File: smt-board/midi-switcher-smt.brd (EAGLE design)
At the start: 68.6 x 67.3 mm, 70 parts, among them IC1 PIC16F1825DIL14, IC2 6N138, Q1 MJD122GDPAK, Q2 MJD122GDPAK, Q3 MJD122GDPAK, Q4 MJD122GDPAK, Q5 MJD122GDPAK, Q6 MJD122GDPAK, Q7 MJD122GDPAK, Q8 MJD122GDPAK

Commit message: version 7
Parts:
- D1: device adafruit:SOD-123FL -> adafruit:SMADIODE
- moved C4 1.80 mm to (80.0, 57.1)
- moved R1 1.27 mm to (49.5, 41.9)
- moved R5 1.27 mm to (41.9, 41.9)
- moved D2 1.27 mm to (49.5, 44.5)
- moved R4 1.27 mm to (41.9, 44.5)
- moved D1 0.46 mm to (71.5, 54.9)
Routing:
- net N$3: track 13.8 -> 15.0 mm
- net N$2: track 27.0 -> 28.2 mm
- net N$5: track 14.5 -> 15.8 mm
- net N$39: track 21.8 -> 22.9 mm
- net N$1: track 12.1 -> 13.0 mm
- net N$28: track 9.43 -> 10.3 mm
- net N$17: track 29.5 -> 29.0 mm
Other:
- board text added: "rev 7"
- board text removed: "rev 6"

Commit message: new layout
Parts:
- removed JP18, JP19: (no value), adafruit:1X01
- added D3: 1N4004, jasons_stuff:DO-VERT
- added JP1, JP2, POWER+1, POWER+2, POWER-1, POWER-2: (no value), adafruit:1X01
- added JP3: (no value), pinhead:1X03
- added R22: (no value), rcl:R0805
- added T1: (no value), transistor:SOT23-BEC
- added U$1: 2.1MMJACKTHM, adafruit:PJ-102A
- C4: device rcl:PANASONIC_F -> rcl:E2,5-7
- C5: device rcl:PANASONIC_D -> rcl:E2,5-6
- D1: value (none) -> 1N4004; device adafruit:SMADIODE -> jasons_stuff:DO-VERT
- IC1: value PIC16F1825DIL14 -> PIC16F1825SO14; device jasons_stuff:DIL14 -> jasons_stuff:SO14
- moved OP1+ 69.2 mm to (31.8, 7.62)
- moved PWR 56.6 mm to (88.9, 36.8)
- moved ACT 54.6 mm to (85.1, 36.8)
- moved C2 39.9 mm to (100.3, 15.2), turned to 270 degrees
- moved OP5+ 39.4 mm to (72.4, 7.62)
- moved R4 37.9 mm to (78.7, 35.6), turned to 0 degrees
- moved R1 37.7 mm to (17.8, 21.6)
- moved R5 37.0 mm to (78.7, 38.1), turned to 180 degrees
- moved REG1 35.3 mm to (105.4, 16.5), turned to 180 degrees
- moved C1 35.3 mm to (106.7, 24.1), turned to 180 degrees
- moved D1 34.9 mm to (100.5, 35.3)
- moved R14 34.3 mm to (101.6, 24.1)
- moved C4 33.8 mm to (99.4, 29.5), turned to 180 degrees
- moved D2 32.5 mm to (24.1, 24.1)
- moved MIDI_IN 32.4 mm to (24.1, 33.0)
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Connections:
- removed net N$44: IC1.3, MODE.1, MODE.2
- new net N$32: IC1.4, ICSP.1, MODE.3, MODE.4
- new net N$40: JP1.1, R22.2
- new net N$41: D1.A, D3.C, JP3.2
- new net N$43: D3.A, U$1.TIP
- net 12V: now also JP3.3, POWER+1.1, POWER+2.1; no longer D1.A, JP18.1
- net GND: now also MODE.1, MODE.2, POWER-1.1, POWER-2.1, T1.C, U$1.RING; no longer JP19.1, MODE.3, MODE.4
- net N$16: now also JP2.1, T1.E
- net N$23: now also IC1.3; no longer IC1.6
- net N$34: now also R22.1, T1.B; no longer IC1.4, ICSP.1
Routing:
- net GND: track 195.8 -> 5.80 mm
- net 12V: track 108.1 -> 26.4 mm
- net N$43: track 0.00 -> 54.3 mm
- net N$44: track 39.2 -> 0.00 mm, vias 2 -> 0
- net N$34: track 38.7 -> 1.95 mm, vias 1 -> 0
- net N$32: track 0.00 -> 35.9 mm, vias 0 -> 1
- net N$22: track 15.0 -> 49.6 mm, vias 1 -> 2
- net N$46: track 11.5 -> 36.5 mm, vias 1 -> 2
- net N$16: track 35.2 -> 52.7 mm
- net N$23: track 17.5 -> 34.3 mm, vias 1 -> 2
- net N$17: track 29.0 -> 14.1 mm, vias 1 -> 2
- net N$41: track 0.00 -> 14.2 mm
- net N$8: track 17.5 -> 3.63 mm, vias 2 -> 0
- net N$45: track 16.5 -> 29.4 mm, vias 1 -> 3
- net N$14: track 14.4 -> 4.06 mm, vias 2 -> 0
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- added copper zone on layer 16, net GND
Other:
- board size 68.6 x 67.3 mm -> 104.1 x 35.6 mm
- board text removed: "1"
- board text removed: "DC-IN"
- board text removed: "FREE"
- board text removed: "H"
- board text removed: "MIDI"
- board text removed: "PORTA"
- board text removed: "PORTB"
- board text removed: "PORTC"
- board text removed: "PORTD"
- board text removed: "PORTE"
- board text removed: "PORTF"
- board text removed: "PORTG"
- board text removed: "PORTH"
- board text removed: "SET"
- board text removed: "YOUR"

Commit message: updates
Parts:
- removed ACT, PWR: (no value), led:CHIP-LED0805
- removed JP2: (no value), adafruit:1X01
- removed R4, R5, R6: (no value), rcl:R0805
- removed T1: (no value), transistor:SOT23-BEC
- added CHAIN_PREV: (no value), adafruit:1X01
- added L1, L2: (no value), led:CHIP-LED0805
- added Q9: (no value), transistor:SOT23-BEC
- added R23, R24, R25: (no value), rcl:R0805
- D1: value 1N4004 -> 0805DIODE; device jasons_stuff:DO-VERT -> jasons_stuff:0805DIODE
- D2: value 0805DIODE -> 1N4004; device jasons_stuff:0805DIODE -> jasons_stuff:DO-VERT
- IC1: value PIC16F1825SO14 -> 6N138; device jasons_stuff:SO14 -> optocoupler:DIL08
- IC2: value 6N138 -> PIC16F1825SO14; device optocoupler:DIL08 -> jasons_stuff:SO14
- moved D2 76.4 mm to (99.2, 38.5)
- moved Q1 71.1 mm to (24.1, 16.5)
- moved Q8 71.1 mm to (95.2, 16.5)
- moved D1 65.0 mm to (35.6, 31.8), turned to 0 degrees
- moved Q2 50.8 mm to (34.3, 16.5)
- moved Q7 50.8 mm to (85.1, 16.5)
- moved C1 47.0 mm to (60.8, 34.3), turned to 0 degrees
- moved C3 47.0 mm to (106.7, 24.1), turned to 180 degrees
- moved Q3 30.5 mm to (44.5, 16.5)
- moved Q6 30.5 mm to (74.9, 16.5)
- moved R14 30.5 mm to (71.1, 24.1)
- moved R20 30.5 mm to (101.6, 24.1)
- moved IC2 22.9 mm to (67.3, 30.5)
- moved R1 21.8 mm to (35.6, 34.3)
- moved IC1 21.6 mm to (45.7, 30.5)
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- renumbered 12V to OP8+1, JP1 to CHAIN_NEXT, LED1 to L3, LED2 to L4, LED3 to L5, LED4 to L6, LED5 to L10, LED8 to L7, LED_6 to L9, LED_7 to L8, REG1 to IC3
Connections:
- removed net 12V: JP3.3, OP1+.1, OP2+.1, OP3+.1, OP4+.1, OP5+.1, OP7+.1, OP8+.1, OP8+1.1, POWER+1.1, POWER+2.1
- removed net N$11 (its old number): Q4.1, R21.1
- removed net N$17: IC1.2, R4.1
- removed net N$19: IC1.13, ICSP.4, R20.1, R21.2
- removed net N$2 (its old number): D2.A, IC2.2, R1.1
- removed net N$20: IC1.8, R12.1, R13.2
- removed net N$21: IC1.7, R10.1, R11.2
- removed net N$22: IC1.9, R8.1, R9.2
- removed net N$23: IC1.3, R6.1, R7.2
- removed net N$32: IC1.4, ICSP.1, MODE.3, MODE.4
- removed net N$34: R22.1, T1.B
- removed net N$40: CHAIN_NEXT.1, R22.2
- removed net N$41: D1.A, D3.C, JP3.2
- removed net N$45: IC1.11, R16.1, R17.2
- removed net N$46: IC1.10, R14.1, R15.2
- removed net VDD: C2.1, C3.2, C5.+, IC1.1, IC2.8, IC3.2, ICSP.2, R3.1, R5.2
- new net +12V: JP3.2, JP3.3, OP1+.1, OP2+.1, OP3+.1, OP4+.1, OP5+.1, OP7+.1, OP8+.1, OP8+1.1, POWER+1.1, POWER+2.1
- new net +5V: C1.2, C2.1, C5.+, IC1.8, IC2.1, IC3.2, ICSP.2, L2.A, R22.2
- new net ACT_LED: IC2.3, L1.A
- new net MIDI_IN: CHAIN_NEXT.1, IC1.6, IC2.12, ICSP.5, Q9.E, R22.1
- new net N$1: D1.C, IC1.3, MIDI_IN.5
- new net N$12: Q4.1, R11.1
- new net N$51: IC2.13, ICSP.4
- new net N$54: D2.C, D3.A, JP3.1
- new net OUT1: IC2.2, R19.2, R20.1
- new net OUT2: IC2.5, R17.2, R18.1
- new net OUT3: IC2.9, R15.2, R16.1
- new net OUT4: IC2.11, R13.2, R14.1
- new net OUT5: IC2.6, R11.2, R12.1
- new net OUT6: IC2.7, R10.1, R9.2
- new net OUT7: IC2.8, R7.2, R8.1
- new net OUT8: IC2.10, R2.2, R3.1
- new net SWITCH: IC2.4, ICSP.1, MODE.1, MODE.2
- net GND: now also IC1.5, IC2.14, MODE.3, MODE.4, Q9.C, R21.1, R24.2, R25.2; no longer ACT.C, IC1.14, IC2.5, MODE.1, MODE.2, PWR.C, R2.1, T1.C
- net N$10: now also Q6.1, R15.1; no longer Q3.1, R19.1
- net N$13: now also Q3.1, R9.1; no longer Q6.1, R11.1
- net N$14: now also Q2.1, R7.1; no longer Q7.1, R9.1
- net N$15: now also Q1.1, R2.1; no longer Q8.1, R7.1
- net N$16: now also Q9.B, R23.2; no longer IC1.5, IC2.6, JP2.1, R3.2, T1.E
- net N$18: now also CHAIN_PREV.1, R23.1; no longer IC1.12, ICSP.5, R18.1, R19.2
- net N$24: now also R16.2; no longer R18.2
- net N$25: now also Q8.2; no longer Q1.2
- net N$26: now also Q7.2; no longer Q2.2
- net N$27: now also Q6.2; no longer Q3.2
- net N$28: now also L2.C, R24.1; no longer PWR.A, R5.1
- net N$29: now also Q4.2; no longer Q5.2
- net N$3: now also D1.A, IC1.2, R1.1; no longer D2.C, IC2.3, MIDI_IN.5
- net N$30: now also Q3.2; no longer Q6.2
- net N$31: now also Q5.2; no longer Q4.2
- net N$33: now also R14.2; no longer R20.2
- net N$38: now also R3.2; no longer R6.2
- net N$39: now also C3.2, D3.C; no longer C1.2, D1.C
- net N$4: now also IC1.7, R21.2; no longer IC2.7, R2.2
- net N$42: now also Q2.2; no longer Q7.2
- net N$43: now also D2.A; no longer D3.A
- net N$47: now also Q1.2; no longer Q8.2
- net N$5: now also L1.C, R25.1; no longer ACT.A, R4.2
- net N$6: now also R20.2; no longer R14.2
- net N$7: now also R18.2; no longer R16.2
- net N$8: now also Q8.1, R19.1; no longer Q1.1, R15.1
- net N$9: now also Q7.1; no longer Q2.1
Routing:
- net VDD: track 120.0 -> 0.00 mm, vias 4 -> 0
- net +5V: track 0.00 -> 109.7 mm, vias 0 -> 3
- net N$22: track 49.6 -> 0.00 mm, vias 2 -> 0
- net N$16: track 52.7 -> 3.60 mm, vias 1 -> 0
- net SWITCH: track 0.00 -> 44.5 mm, vias 0 -> 1
- net OUT7: track 0.00 -> 44.1 mm, vias 0 -> 2
- net MIDI_IN: track 0.00 -> 43.5 mm, vias 0 -> 2
- net OUT1: track 0.00 -> 42.4 mm, vias 0 -> 2
- net OUT8: track 0.00 -> 41.1 mm, vias 0 -> 2
- net N$46: track 36.5 -> 0.00 mm, vias 2 -> 0
- net N$21: track 36.4 -> 0.00 mm, vias 2 -> 0
- net N$32: track 35.9 -> 0.00 mm, vias 1 -> 0
- net N$19: track 35.4 -> 0.00 mm
- net N$23: track 34.3 -> 0.00 mm, vias 2 -> 0
- net N$2 (its old number): track 31.3 -> 0.00 mm
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- added copper zone on layer 16, net +12V
- removed copper zone on layer 16, net 12V
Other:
- board text added: "ACT"
- board text added: "ISP"
- board text added: "MODE"
- board text added: "Outputs"
- board text added: "PWR"
- board text added: "PWR SEL"
- board text added: "R7- R20"
- board text added: "REV7"
- board text added: "six4pix.com/switcher"
- board text added: "~"

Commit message: tidy
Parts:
- moved C2 2.54 mm to (100.3, 12.7), turned to 270 degrees
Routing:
- net +5V: track 109.7 -> 111.3 mm
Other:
- board text added: "H"
- board text added: "ICSP"
- board text removed: "ISP"
- board text removed: "rev 7"
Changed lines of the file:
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@@
 <board>
 <plain>
-<text x="183.6371" y="36.4045" size="1.4224" layer="51" font="vector">rev 7</text>
 <rectangle x1="101.55555" y1="16.56715" x2="105.82275" y2="16.60525" layer="52" rot="R180"/>
 <rectangle x1="79.57185" y1="16.56715" x2="96.37395" y2="16.60525" layer="52" rot="R180"/>
@@
 <rectangle x1="85.40115" y1="19.65325" x2="85.47735" y2="19.69135" layer="52" rot="R180"/>
 <rectangle x1="88.98255" y1="19.69135" x2="89.02065" y2="19.72945" layer="52" rot="R180"/>
-<text x="173.7311" y="45.1675" size="1.4224" layer="51" font="vector">hotchk155</text>
 <wire x1="13.97" y1="5.08" x2="115.57" y2="5.08" width="0.4064" layer="20"/>
 <wire x1="116.84" y1="6.35" x2="116.84" y2="39.37" width="0.4064" layer="20"/>
@@
 <text x="48.641" y="12.065" size="2.54" layer="51" font="vector">~</text>
 <text x="58.801" y="12.065" size="2.54" layer="51" font="vector">~</text>
-<text x="13.335" y="18.034" size="1.27" layer="25" font="vector">Outputs</text>
+<text x="13.335" y="18.288" size="1.27" layer="25" font="vector">Outputs</text>
 <circle x="49.022" y="39.497" radius="0.523634375" width="0.3048" layer="21"/>
-<text x="66.421" y="36.83" size="1.27" layer="25" font="vector" rot="R90">ISP</text>
+<text x="66.294" y="35.814" size="1.27" layer="25" font="vector" rot="R90">ICSP</text>
 <wire x1="95.885" y1="39.116" x2="95.885" y2="35.306" width="0.3048" layer="21"/>
 <wire x1="95.885" y1="35.306" x2="96.393" y2="35.306" width="0.3048" layer="21"/>
@@
 <text x="93.345" y="13.97" size="1.778" layer="22" font="vector" rot="MR0">hotchk155</text>
 <text x="49.53" y="13.97" size="1.778" layer="22" font="vector" rot="MR0">six4pix.com/switcher</text>
+<text x="99.441" y="15.494" size="2.54" layer="51" font="vector">H</text>
 </plain>
 <attributes>
@@
 <attribute name="VALUE" x="58.166" y="34.8488" size="1.27" layer="27" ratio="10" rot="R180"/>
 </element>
-<element name="C2" library="rcl" package="C0805" value="" x="100.33" y="15.24" smashed="yes" rot="R90">
-<attribute name="NAME" x="101.346" y="13.081" size="1.27" layer="25" ratio="10" rot="R180"/>
-<attribute name="VALUE" x="103.124" y="12.954" size="1.27" layer="27" ratio="10" rot="R90"/>
+<element name="C2" library="rcl" package="C0805" value="" x="100.33" y="12.7" smashed="yes" rot="R270">
+<attribute name="NAME" x="101.473" y="9.906" size="1.27" layer="25" ratio="10" rot="R180"/>
+<attribute name="VALUE" x="97.536" y="14.986" size="1.27" layer="27" ratio="10" rot="R270"/>
 </element>
 <element name="R19" library="rcl" package="R0805" value="" x="96.52" y="24.13" smashed="yes">
@@
 </element>
 <element name="C5" library="rcl" package="E2,5-6" value="" x="112.649" y="21.971" smashed="yes">
-<attribute name="NAME" x="113.792" y="24.892" size="1.27" layer="25" ratio="10"/>
+<attribute name="NAME" x="113.919" y="17.907" size="1.27" layer="25" ratio="10"/>
 <attribute name="VALUE" x="115.316" y="19.304" size="1.27" layer="27" ratio="10"/>
 </element>
@@
 <contactref element="R22" pad="2"/>
 <wire x1="105.09" y1="16.19" x2="105.41" y2="16.51" width="1.27" layer="1"/>
-<wire x1="105.41" y1="16.51" x2="105.41" y2="14.01" width="1.27" layer="1"/>
+<wire x1="105.41" y1="16.51" x2="105.41" y2="15.24" width="1.27" layer="1"/>
+<wire x1="105.41" y1="15.24" x2="105.41" y2="14.01" width="1.27" layer="1"/>
 <wire x1="111.379" y1="21.971" x2="111.379" y2="18.669" width="1.27" layer="1"/>
 <wire x1="111.379" y1="18.669" x2="109.22" y2="16.51" width="1.27" layer="1"/>
 <wire x1="109.22" y1="16.51" x2="105.41" y2="16.51" width="1.27" layer="1"/>
-<wire x1="105.41" y1="14.01" x2="100.61" y2="14.01" width="1.27" layer="1"/>
-<wire x1="100.61" y1="14.01" x2="100.33" y2="14.29" width="1.27" layer="1"/>
 <wire x1="61.722" y1="34.229" x2="61.783" y2="34.29" width="0.3048" layer="1"/>
 <wire x1="49.53" y1="34.29" x2="51.181" y2="34.29" width="0.8128" layer="1"/>
@@
 <wire x1="89.535" y1="34.29" x2="89.535" y2="37.338" width="0.3048" layer="1"/>
 <wire x1="89.535" y1="37.338" x2="88.993" y2="37.88" width="0.3048" layer="1"/>
+<wire x1="100.33" y1="13.65" x2="104.46" y2="13.65" width="1.27" layer="1"/>
+<wire x1="104.46" y1="13.65" x2="105.41" y2="12.7" width="1.27" layer="1"/>
+<wire x1="105.41" y1="12.7" x2="105.41" y2="14.01" width="1.27" layer="1"/>
 </signal>
 <signal name="N$43">

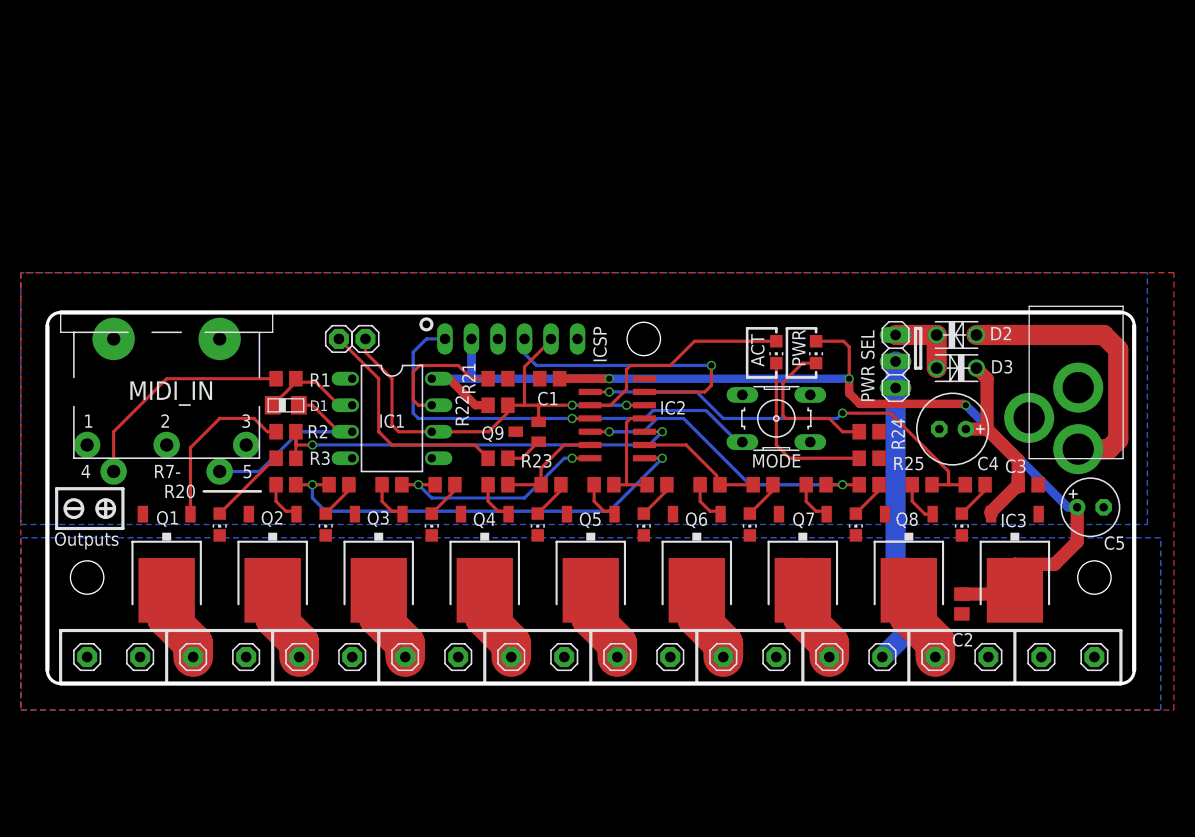
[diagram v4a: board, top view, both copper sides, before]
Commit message: sockets on mm grid
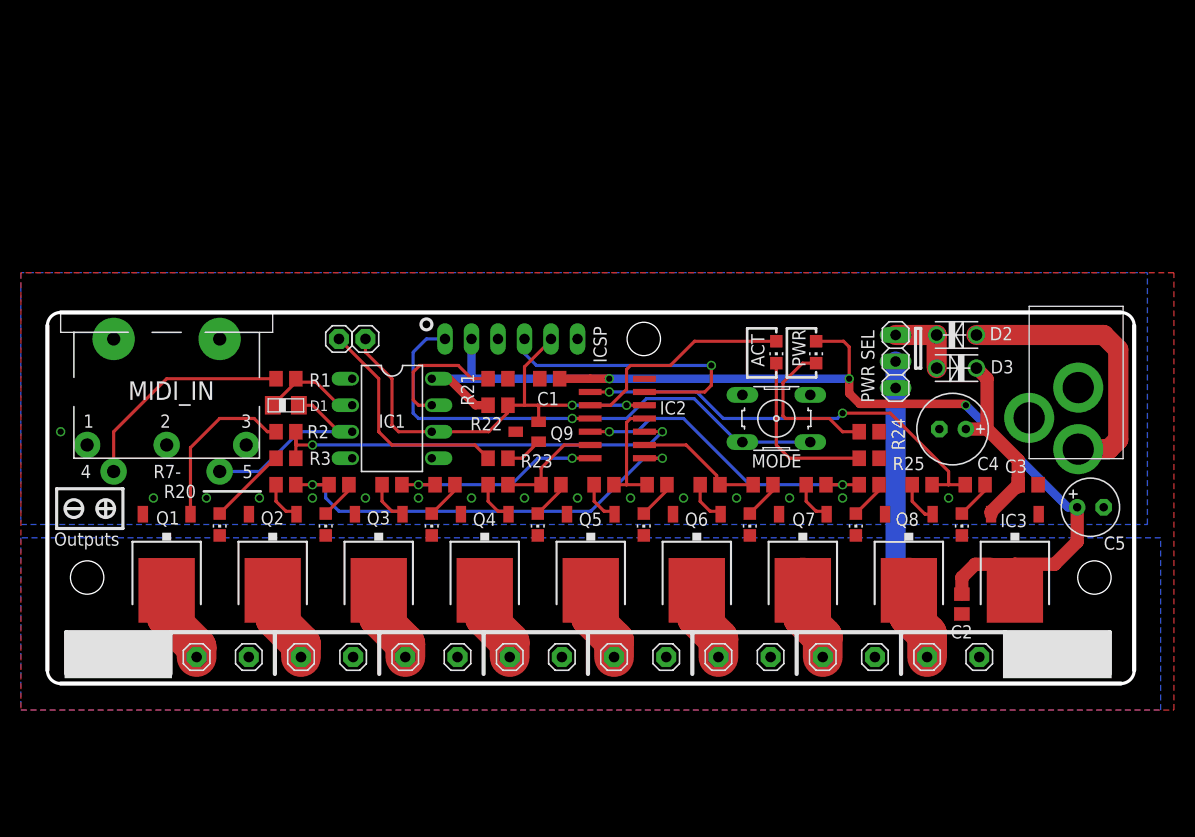
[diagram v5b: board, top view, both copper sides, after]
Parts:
- moved POWER-1 1.03 mm to (112.0, 7.62)
- moved POWER-2 0.95 mm to (107.0, 7.62)
- moved OP2+ 0.87 mm to (102.0, 7.62)
- moved OP1- 0.79 mm to (97.0, 7.62)
- moved OP3+ 0.71 mm to (92.0, 7.62)
- moved OP2- 0.63 mm to (87.0, 7.62)
- moved OP4+ 0.55 mm to (82.0, 7.62)
- moved POWER+2 0.49 mm to (17.0, 7.62)
- moved OP3- 0.47 mm to (77.0, 7.62)
- moved POWER+1 0.41 mm to (22.0, 7.62)
- moved OP5+ 0.39 mm to (72.0, 7.62)
- moved OP8- 0.33 mm to (27.0, 7.62)
- moved OP4- 0.31 mm to (67.0, 7.62)
- moved OP1+ 0.25 mm to (32.0, 7.62)
- moved OP8+1 0.23 mm to (62.0, 7.62)
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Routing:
- net SWITCH: track 44.5 -> 52.5 mm
- net +12V: track 29.9 -> 26.3 mm
- net OUT7: track 44.1 -> 42.3 mm
- net OUT6: track 21.7 -> 20.7 mm
- net +5V: track 111.3 -> 112.1 mm
- net MIDI_IN: track 43.5 -> 44.2 mm
